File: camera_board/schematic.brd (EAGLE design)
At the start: 34 x 25.1 mm, 6 parts

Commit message: Final Schematic Part II
Need to double check and then I'll order boards
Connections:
- removed net N$19: CAMERA1.33
- removed net N$20: CAMERA1.34
- removed net N$21: CAMERA1.16
- removed net N$22: CAMERA1.24
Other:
- board text added: "SPLAM MQP"
- board text removed: "SPLAM MQP - May 2016"
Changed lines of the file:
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@@
 <hole x="31.75" y="2.032" drill="3.2"/>
 <hole x="31.75" y="22.86" drill="3.2"/>
-<text x="29.21" y="0.762" size="1.27" layer="16" rot="MR0">SPLAM MQP - May 2016</text>
 <text x="32.512" y="20.574" size="1.016" layer="26" rot="MR270">LI-VM34LP Breakout</text>
 <text x="31.242" y="20.574" size="1.016" layer="25" rot="R270">LI-VM34LP Breakout</text>
+<text x="22.86" y="0.762" size="1.27" layer="26" rot="MR0">SPLAM MQP</text>
+<text x="12.7" y="0.762" size="1.27" layer="25">SPLAM MQP</text>
 </plain>
 <attributes>
@@
 </class>
 </classes>
-<designrules name="default">
+<designrules name="OSHpark">
 <description language="de">&lt;b&gt;EAGLE Design Rules&lt;/b&gt;
 &lt;p&gt;
@@
 Einstellungen hier und speichern die Design Rules unter
 einem neuen Namen ab.</description>
-<description language="en">&lt;b&gt;EAGLE Design Rules&lt;/b&gt;
+<description language="en">&lt;b&gt;Laen's PCB Order Design Rules&lt;/b&gt;
 &lt;p&gt;
-The default Design Rules have been set to cover
-a wide range of applications. Your particular design
-may have different requirements, so please make the
-necessary adjustments and save your customized
-design rules under a new name.</description>
+Please make sure your boards conform to these design rules.</description>
 <param name="layerSetup" value="(1*16)"/>
-<param name="mtCopper" value="0.035mm 0.035mm 0.035mm 0.035mm 0.035mm 0.035mm 0.035mm 0.035mm 0.035mm 0.035mm 0.035mm 0.035mm 0.035mm 0.035mm 0.035mm 0.035mm"/>
-<param name="mtIsolate" value="1.5mm 0.15mm 0.2mm 0.15mm 0.2mm 0.15mm 0.2mm 0.15mm 0.2mm 0.15mm 0.2mm 0.15mm 0.2mm 0.15mm 0.2mm"/>
-<param name="mdWireWire" value="8mil"/>
-<param name="mdWirePad" value="8mil"/>
-<param name="mdWireVia" value="8mil"/>
-<param name="mdPadPad" value="8mil"/>
-<param name="mdPadVia" value="8mil"/>
-<param name="mdViaVia" value="8mil"/>
-<param name="mdSmdPad" value="8mil"/>
-<param name="mdSmdVia" value="8mil"/>
-<param name="mdSmdSmd" value="8mil"/>
+<param name="mtCopper" value="0.0356mm 0.0356mm 0.0356mm 0.0356mm 0.0356mm 0.0356mm 0.0356mm 0.0356mm 0.0356mm 0.0356mm 0.0356mm 0.0356mm 0.0356mm 0.0356mm 0.0356mm 0.0356mm"/>
+<param name="mtIsolate" value="1.5011mm 0.1499mm 0.2007mm 0.1499mm 0.2007mm 0.1499mm 0.2007mm 0.1499mm 0.2007mm 0.1499mm 0.2007mm 0.1499mm 0.2007mm 0.1499mm 0.2007mm"/>
+<param name="mdWireWire" value="6mil"/>
+<param name="mdWirePad" value="6mil"/>
+<param name="mdWireVia" value="6mil"/>
+<param name="mdPadPad" value="6mil"/>
+<param name="mdPadVia" value="6mil"/>
+<param name="mdViaVia" value="6mil"/>
+<param name="mdSmdPad" value="6mil"/>
+<param name="mdSmdVia" value="6mil"/>
+<param name="mdSmdSmd" value="6mil"/>
 <param name="mdViaViaSameLayer" value="8mil"/>
 <param name="mnLayersViaInSmd" value="2"/>
-<param name="mdCopperDimension" value="40mil"/>
-<param name="mdDrill" value="8mil"/>
+<param name="mdCopperDimension" value="15mil"/>
+<param name="mdDrill" value="6mil"/>
 <param name="mdSmdStop" value="0mil"/>
-<param name="msWidth" value="10mil"/>
-<param name="msDrill" value="24mil"/>
-<param name="msMicroVia" value="9.99mm"/>
+<param name="msWidth" value="6mil"/>
+<param name="msDrill" value="13mil"/>
+<param name="msMicroVia" value="13mil"/>
 <param name="msBlindViaRatio" value="0.5"/>
 <param name="rvPadTop" value="0.25"/>
@@
 <param name="rvMicroViaOuter" value="0.25"/>
 <param name="rvMicroViaInner" value="0.25"/>
-<param name="rlMinPadTop" value="10mil"/>
+<param name="rlMinPadTop" value="7mil"/>
 <param name="rlMaxPadTop" value="20mil"/>
-<param name="rlMinPadInner" value="10mil"/>
+<param name="rlMinPadInner" value="7mil"/>
 <param name="rlMaxPadInner" value="20mil"/>
-<param name="rlMinPadBottom" value="10mil"/>
+<param name="rlMinPadBottom" value="7mil"/>
 <param name="rlMaxPadBottom" value="20mil"/>
-<param name="rlMinViaOuter" value="8mil"/>
+<param name="rlMinViaOuter" value="7mil"/>
 <param name="rlMaxViaOuter" value="20mil"/>
-<param name="rlMinViaInner" value="8mil"/>
+<param name="rlMinViaInner" value="7mil"/>
 <param name="rlMaxViaInner" value="20mil"/>
 <param name="rlMinMicroViaOuter" value="4mil"/>
@@
 <param name="mvStopFrame" value="1"/>
 <param name="mvCreamFrame" value="0"/>
-<param name="mlMinStopFrame" value="4mil"/>
-<param name="mlMaxStopFrame" value="4mil"/>
+<param name="mlMinStopFrame" value="3mil"/>
+<param name="mlMaxStopFrame" value="3mil"/>
 <param name="mlMinCreamFrame" value="0mil"/>
 <param name="mlMaxCreamFrame" value="0mil"/>
@@
 <contactref element="PWR2" pad="1"/>
 <wire x1="14.986" y1="12.573" x2="14.986" y2="13.97" width="0.3048" layer="16"/>
-<wire x1="14.986" y1="13.97" x2="16.51" y2="15.494" width="0.3048" layer="16"/>
-<wire x1="16.51" y1="15.494" x2="19.812" y2="15.494" width="0.3048" layer="16"/>
-<via x="19.812" y="15.494" extent="1-16" drill="0.6" shape="octagon"/>
-<wire x1="19.812" y1="15.494" x2="23.876" y2="19.558" width="0.3048" layer="1"/>
+<wire x1="14.986" y1="13.97" x2="16.764" y2="15.24" width="0.3048" layer="16"/>
+<wire x1="16.764" y1="15.24" x2="19.558" y2="15.24" width="0.3048" layer="16"/>
+<via x="19.558" y="15.24" extent="1-16" drill="0.6" shape="octagon"/>
+<wire x1="19.558" y1="15.24" x2="23.876" y2="19.558" width="0.3048" layer="1"/>
 <wire x1="23.876" y1="19.558" x2="25.781" y2="19.558" width="0.3048" layer="1"/>
 </signal>
@@
 <wire x1="21.336" y1="9.398" x2="21.336" y2="11.303" width="0.3048" layer="16"/>
 </signal>
-<signal name="N$19">
-<contactref element="CAMERA1" pad="33"/>
-</signal>
-<signal name="N$20">
-<contactref element="CAMERA1" pad="34"/>
-</signal>
-<signal name="N$21">
-<contactref element="CAMERA1" pad="16"/>
-</signal>
-<signal name="N$22">
-<contactref element="CAMERA1" pad="24"/>
-</signal>
 <signal name="N$23">

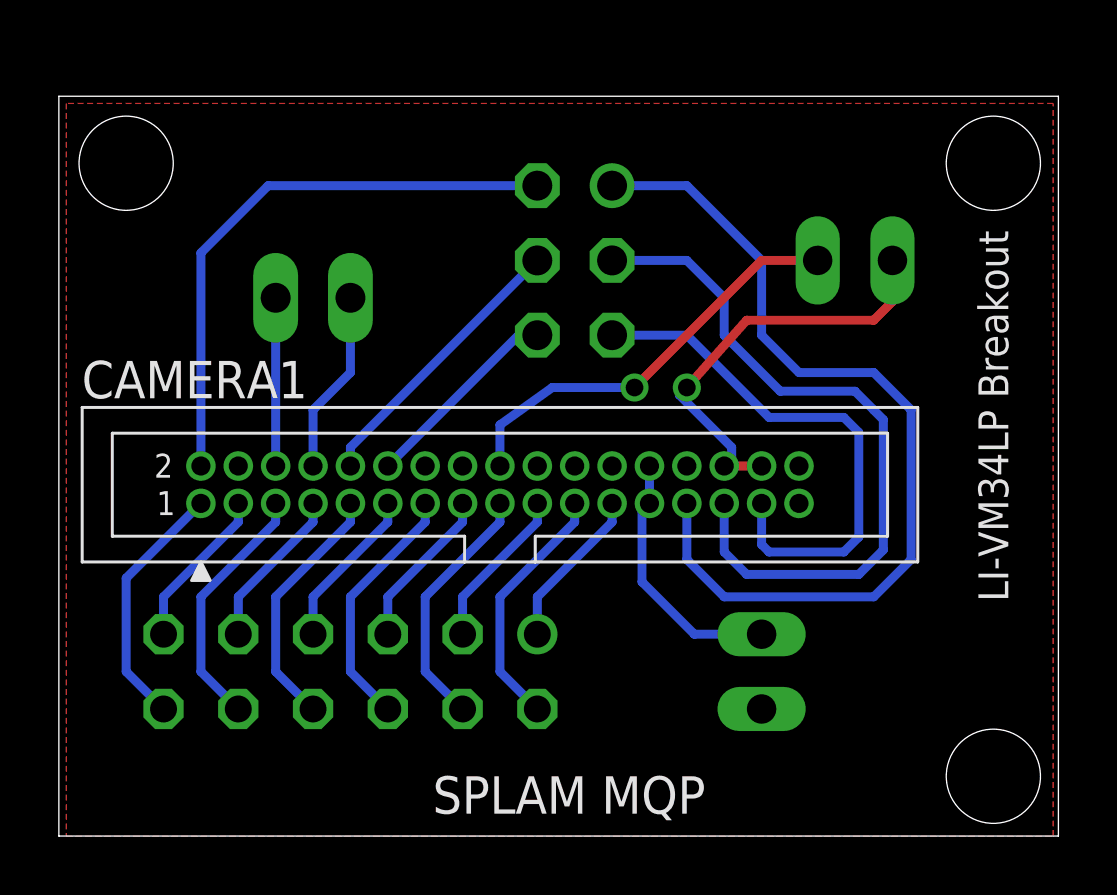
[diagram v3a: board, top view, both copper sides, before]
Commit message: Added missing pin, finalized(?) board design
- Missed the trigger pin, that could have been bad!
- Double checked the layout and it looks correct
- Passed OSHpark DRC, ERC
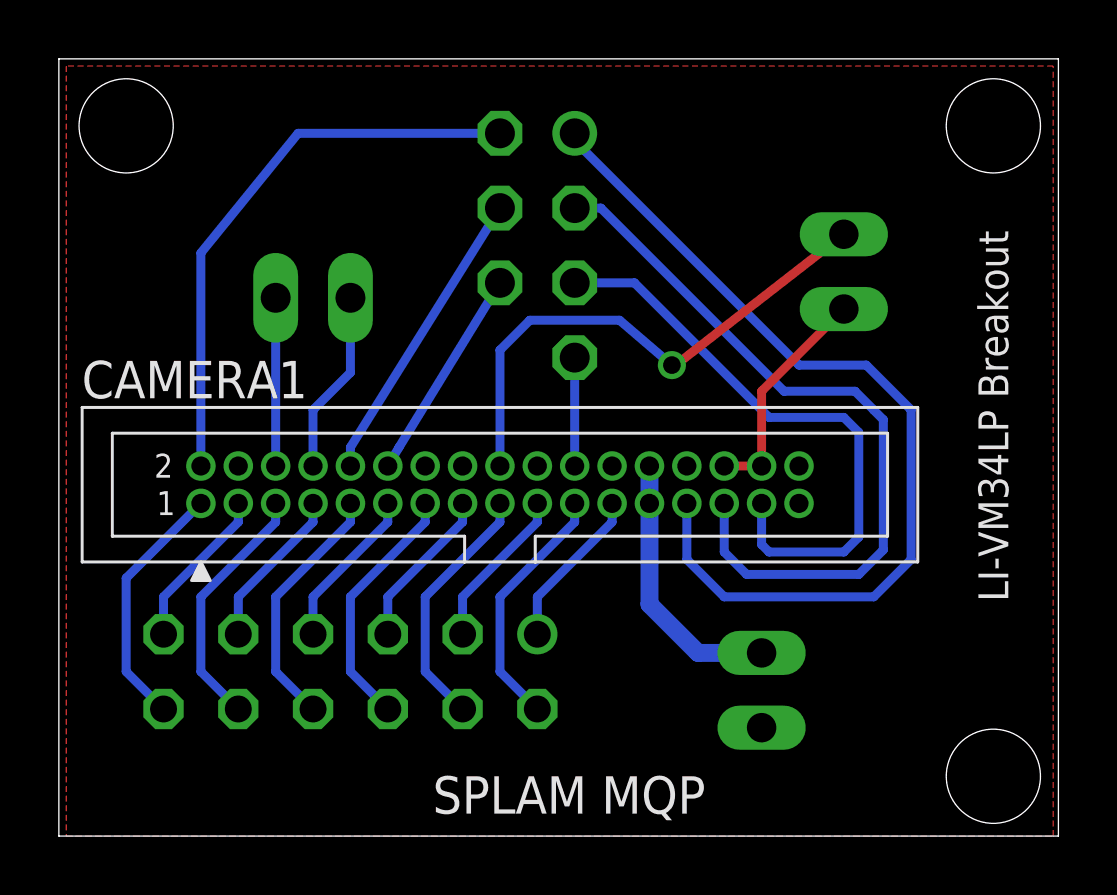
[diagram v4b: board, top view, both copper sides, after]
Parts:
- removed POWER1: MAIN, con-molex:22-23-2021
- added POWER: MAIN, con-molex:22-23-2021
- added TRIG: (no value), pinhead:1X01
- moved CONTROL 2.18 mm to (16.3, 21.3)
- moved PWR2 0.54 mm to (26.7, 19.2), turned to 270 degrees
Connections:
- net GND: now also POWER.1; no longer POWER1.1
- net TRIGGER: now also TRIG.1
- net VCC: now also POWER.2; no longer POWER1.2
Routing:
- net 1.8V: track 14.6 -> 7.76 mm, vias 1 -> 0
- net 2.8V: track 14.4 -> 18.1 mm
- net TRIGGER: track 0.00 -> 3.68 mm
- net N$16: track 18.3 -> 20.3 mm
- net N$17: track 24.3 -> 25.6 mm
- net N$18: track 30.5 -> 31.1 mm
- net N$14: track 9.62 -> 10.2 mm
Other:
- board size 34 x 25.1 mm -> 34 x 26.4 mm
